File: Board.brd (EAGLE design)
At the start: 47 x 35 mm, 56 parts, among them IC1 CP210X_USB_UART, T1 BC846, T2 BC846

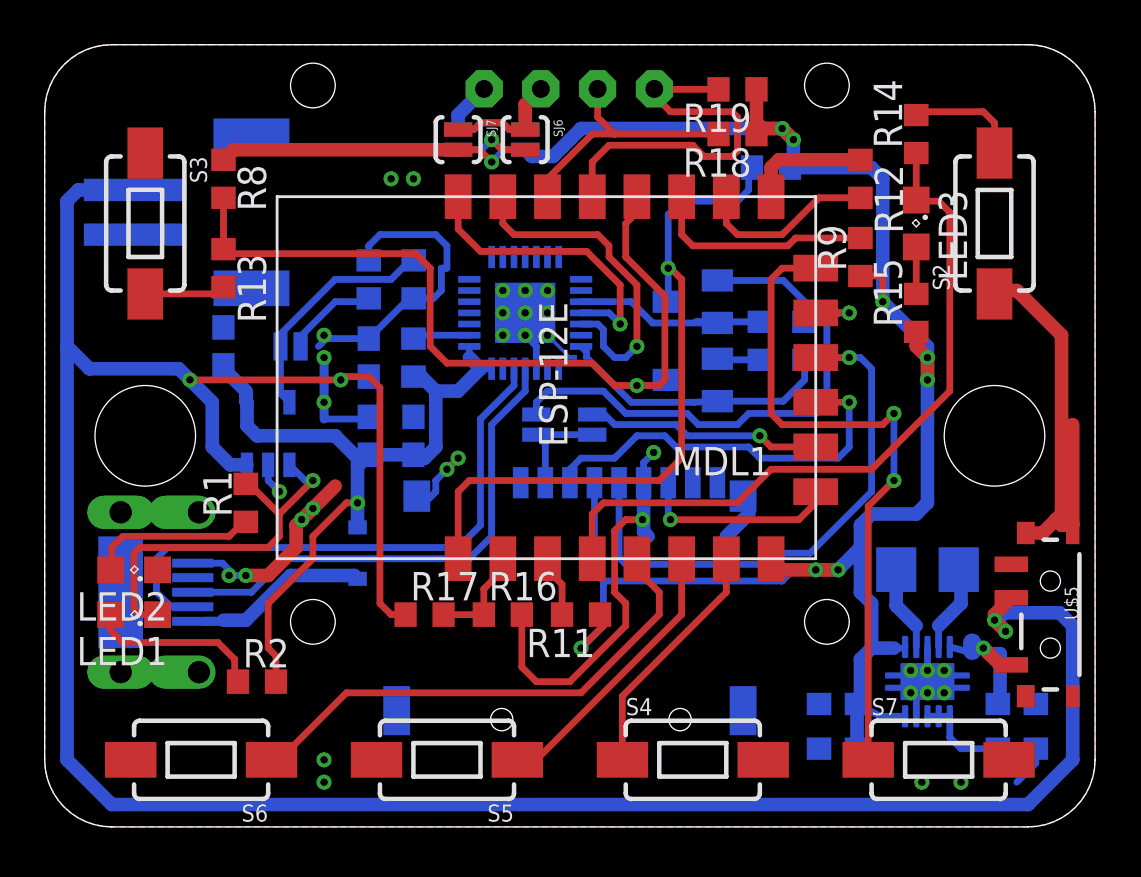
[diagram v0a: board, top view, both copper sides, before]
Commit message: placed silkscreen
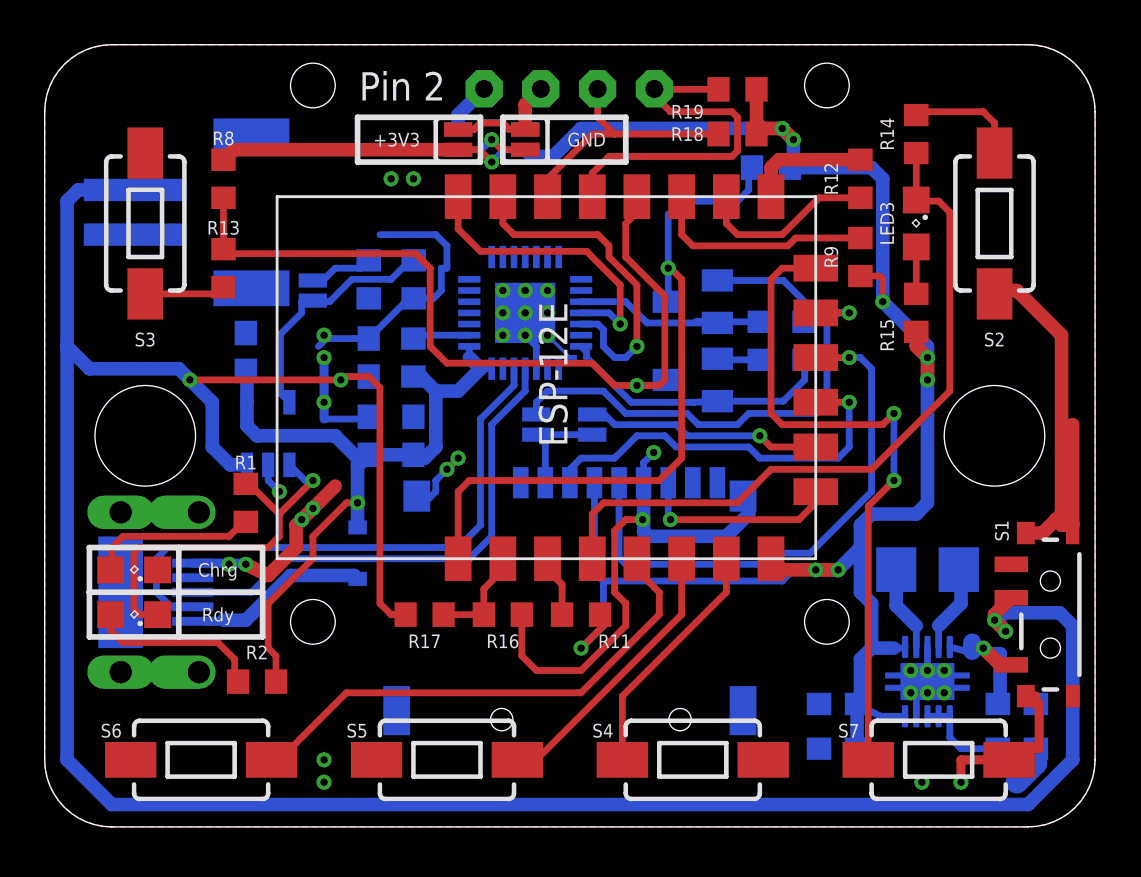
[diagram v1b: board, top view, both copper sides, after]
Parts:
- added S1: SPDT_GROUNDED, SparkFun-Electromechanical:SWITCH-SPST-SMD-A
- U$5: value SPDT_GROUNDED -> (none); device SparkFun-Electromechanical:SWITCH-SPST-SMD-A -> OwnStuff:LOGO-SILKSCREEN
- moved U$5 18.2 mm to (42.0, 27.5), flipped to the bottom, turned to 90 degrees
- moved SJ1 2.69 mm to (12.0, 24.0), turned to 90 degrees
- moved C5 1.03 mm to (9.00, 21.2)
- turned R3 to 90 degrees
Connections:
- net GND: now also S1.GND1, S1.GND2, S1.GND3, S1.GND4; no longer U$5.GND1, U$5.GND2, U$5.GND3, U$5.GND4
- net N$17: now also S1.3; no longer U$5.3
- net V+: now also S1.2; no longer U$5.2
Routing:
- net GND: track 88.4 -> 97.5 mm
- net N$12: track 4.19 -> 2.87 mm
- net SDA: track 17.5 -> 16.8 mm
- net +5V: track 33.7 -> 33.1 mm
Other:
- board text added: "+3V3"
- board text added: "CP2102"
- board text added: "Chrg"
- board text added: "Fast Charge"
- board text added: "GND"
- board text added: "HW CS"
- board text added: "MCP73831"
- board text added: "Pin 2"
- board text added: "Pin1"
- board text added: "Rdy"
- board text added: "SW CS"

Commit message: added lables for navigation buttons
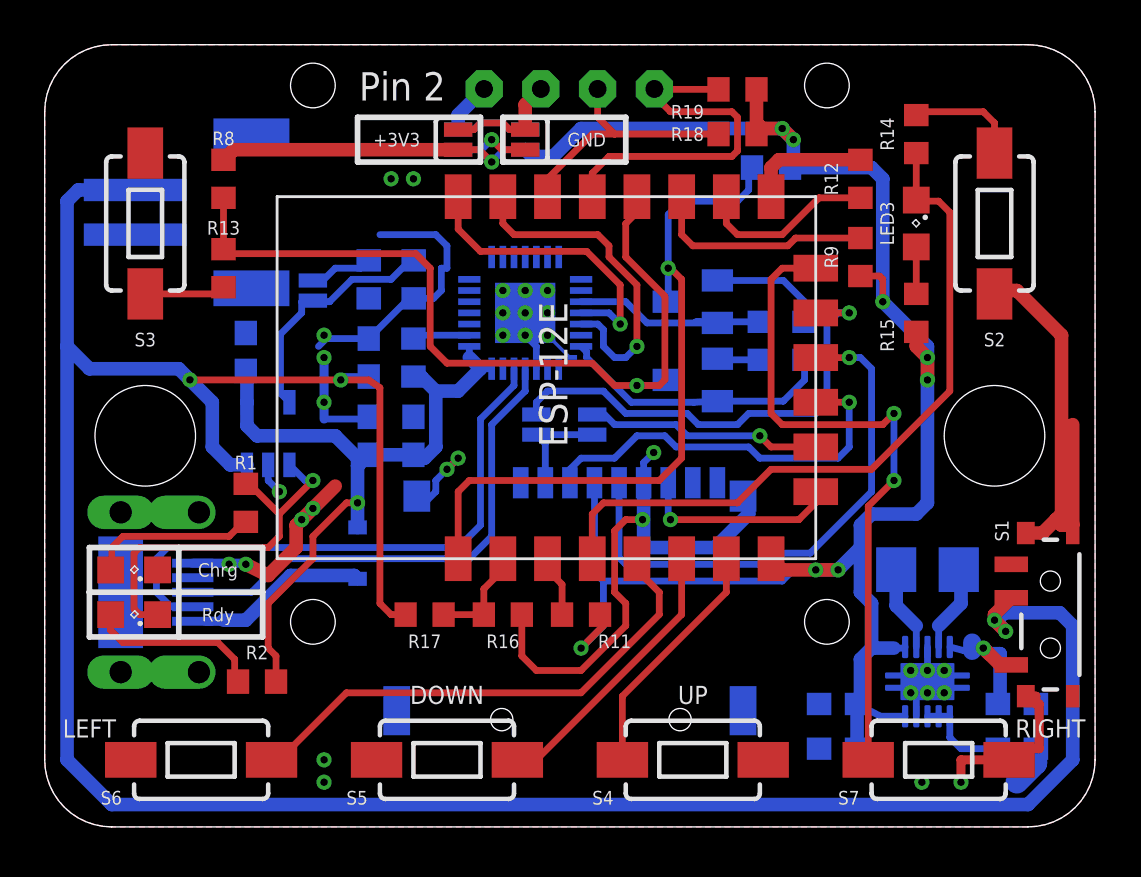
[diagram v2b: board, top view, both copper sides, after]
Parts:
- S4: value DOWN -> UP
- S5: value UP -> DOWN
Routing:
- net GND: track 97.5 -> 98.2 mm
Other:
- board text added: "DOWN"
- board text added: "LEFT"
- board text added: "RIGHT"
- board text added: "UP"
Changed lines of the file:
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@@
 <grid distance="0.5" unitdist="mm" unit="mm" style="lines" multiple="1" display="yes" altdistance="0.25" altunitdist="mm" altunit="mm"/>
 <layers>
-<layer number="1" name="Top" color="4" fill="1" visible="no" active="yes"/>
+<layer number="1" name="Top" color="4" fill="1" visible="yes" active="yes"/>
 <layer number="2" name="Route2" color="1" fill="3" visible="yes" active="yes"/>
 <layer number="3" name="Route3" color="4" fill="3" visible="yes" active="yes"/>
@@
 <layer number="17" name="Pads" color="2" fill="1" visible="yes" active="yes"/>
 <layer number="18" name="Vias" color="2" fill="1" visible="yes" active="yes"/>
-<layer number="19" name="Unrouted" color="6" fill="1" visible="no" active="yes"/>
+<layer number="19" name="Unrouted" color="6" fill="1" visible="yes" active="yes"/>
 <layer number="20" name="Dimension" color="15" fill="1" visible="yes" active="yes"/>
-<layer number="21" name="tPlace" color="7" fill="1" visible="no" active="yes"/>
+<layer number="21" name="tPlace" color="7" fill="1" visible="yes" active="yes"/>
 <layer number="22" name="bPlace" color="7" fill="1" visible="yes" active="yes"/>
-<layer number="23" name="tOrigins" color="15" fill="1" visible="no" active="yes"/>
-<layer number="24" name="bOrigins" color="15" fill="1" visible="no" active="yes"/>
-<layer number="25" name="tNames" color="7" fill="1" visible="no" active="yes"/>
+<layer number="23" name="tOrigins" color="15" fill="1" visible="yes" active="yes"/>
+<layer number="24" name="bOrigins" color="15" fill="1" visible="yes" active="yes"/>
+<layer number="25" name="tNames" color="7" fill="1" visible="yes" active="yes"/>
 <layer number="26" name="bNames" color="7" fill="1" visible="yes" active="yes"/>
 <layer number="27" name="tValues" color="7" fill="1" visible="no" active="yes"/>
 <layer number="28" name="bValues" color="7" fill="1" visible="no" active="yes"/>
-<layer number="29" name="tStop" color="7" fill="3" visible="no" active="yes"/>
+<layer number="29" name="tStop" color="7" fill="3" visible="yes" active="yes"/>
 <layer number="30" name="bStop" color="7" fill="6" visible="no" active="yes"/>
 <layer number="31" name="tCream" color="7" fill="4" visible="no" active="yes"/>
@@
 <layer number="43" name="vRestrict" color="2" fill="10" visible="no" active="yes"/>
 <layer number="44" name="Drills" color="7" fill="1" visible="no" active="yes"/>
-<layer number="45" name="Holes" color="7" fill="1" visible="no" active="yes"/>
+<layer number="45" name="Holes" color="7" fill="1" visible="yes" active="yes"/>
 <layer number="46" name="Milling" color="3" fill="1" visible="no" active="yes"/>
 <layer number="47" name="Measures" color="7" fill="1" visible="no" active="yes"/>
@@
 <wire x1="29.25" y1="17" x2="23" y2="17" width="0.254" layer="22"/>
 <text x="27.25" y="18" size="0.6096" layer="22" rot="MR0" align="center">SW CS</text>
+<text x="2" y="4" size="0.8128" layer="25" align="bottom-center">LEFT</text>
+<text x="18" y="5.5" size="0.8128" layer="25" align="bottom-center">DOWN</text>
+<text x="29" y="5.5" size="0.8128" layer="25" align="bottom-center">UP</text>
+<text x="45" y="4" size="0.8128" layer="25" align="bottom-center">RIGHT</text>
 </plain>
 <attributes>
@@
 <attribute name="VALUE" x="1.8" y="30" size="0.762" layer="27" rot="R270"/>
 </element>
-<element name="S4" library="SparkFun-Electromechanical" package="TACTILE-SWITCH-1101NE" value="DOWN" x="29" y="3" smashed="yes">
+<element name="S4" library="SparkFun-Electromechanical" package="TACTILE-SWITCH-1101NE" value="UP" x="29" y="3" smashed="yes">
 <attribute name="PROD_ID" value="SWCH-00815" x="29" y="3" size="1.778" layer="27" display="off"/>
-<attribute name="NAME" x="24.5" y="4" size="0.6096" layer="25"/>
+<attribute name="NAME" x="24.5" y="1" size="0.6096" layer="25"/>
 <attribute name="VALUE" x="26" y="0.3" size="0.762" layer="27"/>
 </element>
-<element name="S5" library="SparkFun-Electromechanical" package="TACTILE-SWITCH-1101NE" value="UP" x="18" y="3" smashed="yes" rot="R180">
+<element name="S5" library="SparkFun-Electromechanical" package="TACTILE-SWITCH-1101NE" value="DOWN" x="18" y="3" smashed="yes" rot="R180">
 <attribute name="PROD_ID" value="SWCH-00815" x="18" y="3" size="1.778" layer="27" rot="R180" display="off"/>
-<attribute name="NAME" x="13.5" y="4" size="0.6096" layer="25"/>
+<attribute name="NAME" x="13.5" y="1" size="0.6096" layer="25"/>
 <attribute name="VALUE" x="21" y="5.7" size="0.762" layer="27" rot="R180"/>
 </element>
 <element name="S6" library="SparkFun-Electromechanical" package="TACTILE-SWITCH-1101NE" value="LEFT" x="7" y="3" smashed="yes" rot="R180">
 <attribute name="PROD_ID" value="SWCH-00815" x="7" y="3" size="1.778" layer="27" rot="R180" display="off"/>
-<attribute name="NAME" x="2.5" y="4" size="0.6096" layer="25"/>
+<attribute name="NAME" x="2.5" y="1" size="0.6096" layer="25"/>
 <attribute name="VALUE" x="10" y="5.7" size="0.762" layer="27" rot="R180"/>
 </element>
 <element name="S7" library="SparkFun-Electromechanical" package="TACTILE-SWITCH-1101NE" value="RIGHT" x="40" y="3" smashed="yes">
 <attribute name="PROD_ID" value="SWCH-00815" x="40" y="3" size="1.778" layer="27" display="off"/>
-<attribute name="NAME" x="35.5" y="4" size="0.6096" layer="25"/>
+<attribute name="NAME" x="35.5" y="1" size="0.6096" layer="25"/>
 <attribute name="VALUE" x="37" y="0.3" size="0.762" layer="27"/>
 </element>
@@
 <wire x1="18.5" y1="16.5" x2="18" y2="16" width="0.3048" layer="16"/>
 <wire x1="18" y1="16" x2="18.5" y2="16.5" width="0.3048" layer="1"/>
-<wire x1="26.8" y1="15.4" x2="26.8" y2="13.2" width="0.6096" layer="16"/>
-<wire x1="26.8" y1="13.2" x2="27" y2="13" width="0.6096" layer="16"/>
-<wire x1="30.5" y1="13" x2="31.5" y2="14" width="0.6096" layer="16"/>
+<wire x1="26.8" y1="15.4" x2="26.8" y2="12.7" width="0.6096" layer="16"/>
+<wire x1="26.8" y1="12.7" x2="27" y2="12.5" width="0.6096" layer="16"/>
+<wire x1="30" y1="12.5" x2="31.5" y2="14" width="0.6096" layer="16"/>
 <wire x1="31.5" y1="14" x2="31.5" y2="14.3" width="0.6096" layer="16"/>
 <wire x1="31.5" y1="14.3" x2="31.25" y2="14.8" width="0.6096" layer="16"/>
@@
 <wire x1="6.625" y1="11.8" x2="8.95" y2="11.8" width="0.4064" layer="16"/>
 <wire x1="8.95" y1="11.8" x2="9" y2="11.75" width="0.4064" layer="16"/>
+<wire x1="30" y1="12.5" x2="27" y2="12.5" width="0.6096" layer="16"/>
 <wire x1="44.35" y1="5.5" x2="44.35" y2="5.5" width="0" layer="19" extent="1-16"/>
-<wire x1="30.5" y1="13" x2="27" y2="13" width="0.6096" layer="16"/>
 </signal>
 <signal name="N$7">
@@
 <wire x1="13.15" y1="20.15" x2="13.25" y2="20" width="0.3048" layer="16"/>
 <via x="13.25" y="20" extent="1-16" drill="0.3302" shape="octagon"/>
-<wire x1="13.25" y1="20" x2="6.5" y2="20" width="0.3048" layer="1"/>
 <via x="6.5" y="20" extent="1-16" drill="0.3302" shape="octagon"/>
+<wire x1="13.15" y1="20" x2="6.5" y2="20" width="0.3048" layer="1"/>
 <wire x1="16.15" y1="9.5" x2="15.5" y2="9.5" width="0.3048" layer="1"/>
 <wire x1="15.5" y1="9.5" x2="15" y2="10" width="0.3048" layer="1"/>
 <wire x1="15" y1="10" x2="15" y2="19.65" width="0.3048" layer="1"/>
-<wire x1="15" y1="19.65" x2="14.5" y2="20.15" width="0.3048" layer="1"/>
-<wire x1="14.5" y1="20.15" x2="13.15" y2="20.15" width="0.3048" layer="1"/>
-<wire x1="13.15" y1="20.15" x2="13.25" y2="20" width="0.3048" layer="1"/>
+<wire x1="15" y1="19.65" x2="14.5" y2="20" width="0.3048" layer="1"/>
+<wire x1="14.5" y1="20" x2="13.15" y2="20" width="0.3048" layer="1"/>
 <contactref element="S1" pad="2"/>
 <wire x1="45.42" y1="9.58" x2="42.94" y2="9.58" width="0.6096" layer="16"/>
@@
 <wire x1="42.5" y1="9.25" x2="42.5" y2="9.5" width="0.6096" layer="1"/>
 <wire x1="42.5" y1="9.5" x2="43.25" y2="10.25" width="0.6096" layer="1"/>
+<wire x1="13.15" y1="20" x2="13.25" y2="20" width="0" layer="19" extent="1-16"/>
 </signal>
 <signal name="N$3">
